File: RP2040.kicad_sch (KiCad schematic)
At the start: 33 parts, among them J1 USB_B_Micro, J2 Conn_01x03, SW1 SW_Push, SW2 SW_Push, U1 AMS1117-3.3, U5 W25Q128JVS, U6 RP2040, Y1 X322512MSB4SI

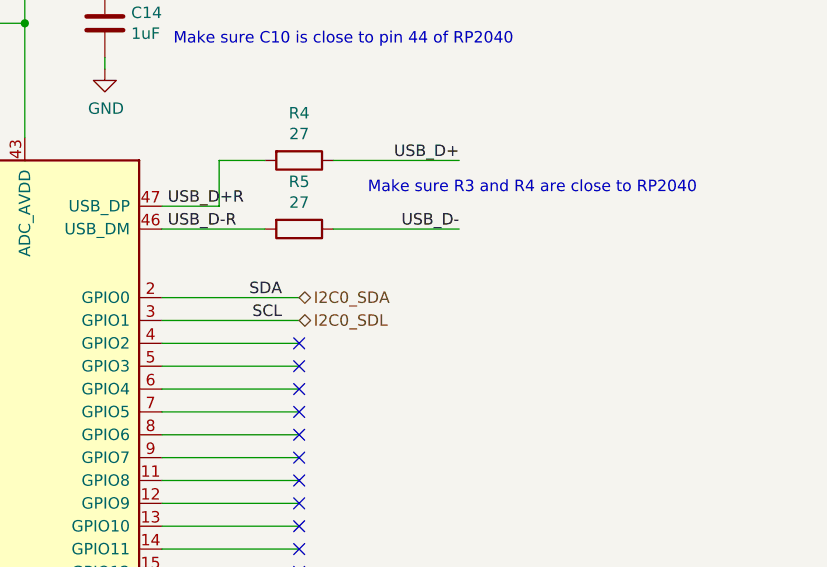
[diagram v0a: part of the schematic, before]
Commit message: Add TCA8418
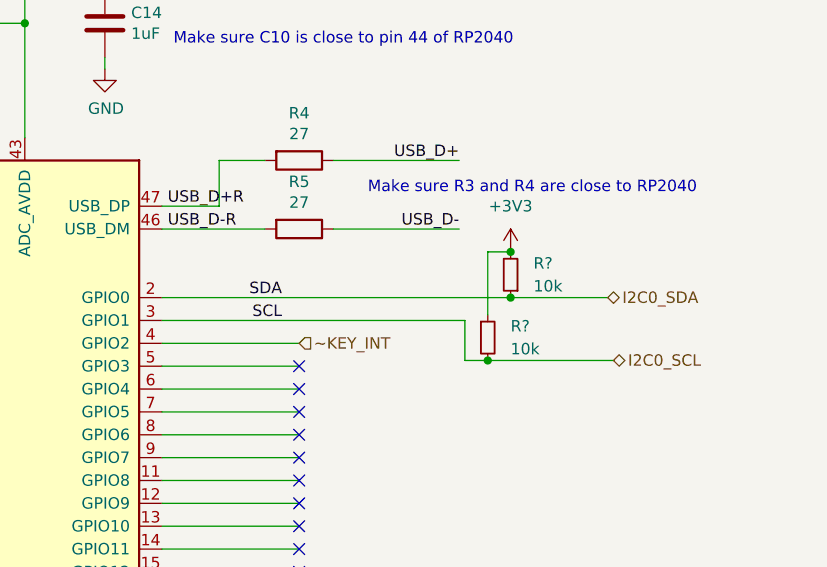
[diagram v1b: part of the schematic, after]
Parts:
- added R? (x2): 10k, symbol Device:R_Small
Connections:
- net +3V3: now also R?.1, R?.2
- net I2C0_SDA: now also R?.1
- net ~KEY_INT: now reaches U6.4 (GPIO2)
- net I2C0_SDL renamed I2C0_SCL
- net I2C0_SCL: now also R?.2
- no-connect marks 29 -> 28
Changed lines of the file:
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@@
   (junction (at 197.485 21.59) (diameter 0) (color 0 0 0 0)
   )
+  (junction (at 248.92 79.375) (diameter 0) (color 0 0 0 0)
+  )
   (junction (at 197.485 41.91) (diameter 0) (color 0 0 0 0)
   )
   (junction (at 182.245 41.91) (diameter 0) (color 0 0 0 0)
   )
+  (junction (at 251.46 72.39) (diameter 0) (color 0 0 0 0)
+  )
   (junction (at 40.005 152.4) (diameter 0) (color 0 0 0 0)
   )
@@
   )
   (junction (at 74.93 65.405) (diameter 0) (color 0 0 0 0)
+  )
+  (junction (at 251.46 67.31) (diameter 0) (color 0 0 0 0)
   )
   (junction (at 263.525 21.59) (diameter 0) (color 0 0 0 0)
@@
   (no_connect (at 29.845 34.925))
   (no_connect (at 227.965 118.11))
-  (no_connect (at 227.965 77.47))
   (no_connect (at 227.965 148.59))
   (no_connect (at 227.965 115.57))
@@
     (stroke (width 0) (type default) (color 0 0 0 0))
   )
-  (wire (pts (xy 212.725 72.39) (xy 227.965 72.39))
+  (wire (pts (xy 212.725 72.39) (xy 251.46 72.39))
     (stroke (width 0) (type default) (color 0 0 0 0))
   )
@@
     (stroke (width 0) (type default) (color 0 0 0 0))
   )
+  (wire (pts (xy 248.92 67.31) (xy 251.46 67.31))
+    (stroke (width 0) (type default) (color 0 0 0 0))
+  )
   (polyline (pts (xy 14.605 107.95) (xy 14.605 130.81))
     (stroke (width 0) (type default) (color 0 0 0 0))
@@
     (stroke (width 0) (type default) (color 0 0 0 0))
   )
+  (wire (pts (xy 251.46 72.39) (xy 262.255 72.39))
+    (stroke (width 0) (type default) (color 0 0 0 0))
+  )
   (wire (pts (xy 219.075 57.15) (xy 224.155 57.15))
     (stroke (width 0) (type default) (color 0 0 0 0))
@@
     (stroke (width 0) (type default) (color 0 0 0 0))
   )
+  (wire (pts (xy 248.92 74.295) (xy 248.92 67.31))
+    (stroke (width 0) (type default) (color 0 0 0 0))
+  )
   (polyline (pts (xy 14.605 103.505) (xy 106.045 103.505))
     (stroke (width 0) (type default) (color 0 0 0 0))
@@
     (stroke (width 0) (type default) (color 0 0 0 0))
   )
+  (wire (pts (xy 246.38 79.375) (xy 248.92 79.375))
+    (stroke (width 0) (type default) (color 0 0 0 0))
+  )
   (wire (pts (xy 19.685 40.005) (xy 19.685 41.275))
     (stroke (width 0) (type default) (color 0 0 0 0))
@@
     (stroke (width 0) (type default) (color 0 0 0 0))
   )
+  (wire (pts (xy 248.92 79.375) (xy 262.89 79.375))
+    (stroke (width 0) (type default) (color 0 0 0 0))
+  )
   (wire (pts (xy 212.725 90.17) (xy 227.965 90.17))
     (stroke (width 0) (type default) (color 0 0 0 0))
@@
     (stroke (width 0) (type default) (color 0 0 0 0))
   )
-  (wire (pts (xy 212.725 74.93) (xy 227.965 74.93))
+  (wire (pts (xy 212.725 74.93) (xy 246.38 74.93))
     (stroke (width 0) (type default) (color 0 0 0 0))
   )
@@
   )
   (wire (pts (xy 212.725 115.57) (xy 227.965 115.57))
+    (stroke (width 0) (type default) (color 0 0 0 0))
+  )
+  (wire (pts (xy 246.38 74.93) (xy 246.38 79.375))
     (stroke (width 0) (type default) (color 0 0 0 0))
   )
@@
     (effects (font (size 1.27 1.27)) (justify left bottom))
   )
-  (hierarchical_label "I2C0_SDA" (shape bidirectional) (at 227.965 72.39 0)
+  (hierarchical_label "~KEY_INT" (shape input) (at 227.965 77.47 0)
     (effects (font (size 1.27 1.27)) (justify left))
   )
-  (hierarchical_label "I2C0_SDL" (shape bidirectional) (at 227.965 74.93 0)
+  (hierarchical_label "I2C0_SDA" (shape bidirectional) (at 262.255 72.39 0)
+    (effects (font (size 1.27 1.27)) (justify left))
+  )
+  (hierarchical_label "I2C0_SCL" (shape bidirectional) (at 262.89 79.375 0)
     (effects (font (size 1.27 1.27)) (justify left))
   )
@@
     )
     (property "Datasheet" "~" (id 3) (at 99.695 138.43 0)
+      (effects (font (size 1.27 1.27)) hide)
+    )
+    (pin "1")
+  )
+  (symbol (lib_id "Device:R_Small") (at 251.46 69.85 180) (unit 1)
+    (in_bom yes) (on_board yes) (fields_autoplaced)
+    (property "Reference" "R?" (id 0) (at 254 68.5799 0)
+      (effects (font (size 1.27 1.27)) (justify right))
+    )
+    (property "Value" "10k" (id 1) (at 254 71.1199 0)
+      (effects (font (size 1.27 1.27)) (justify right))
+    )
+    (property "Footprint" "" (id 2) (at 251.46 69.85 0)
+      (effects (font (size 1.27 1.27)) hide)
+    )
+    (property "Datasheet" "~" (id 3) (at 251.46 69.85 0)
+      (effects (font (size 1.27 1.27)) hide)
+    )
+    (pin "1")
+    (pin "2")
+  )
+  (symbol (lib_id "power:+3V3") (at 251.46 67.31 0) (unit 1)
+    (in_bom yes) (on_board yes) (fields_autoplaced)
+    (property "Reference" "#PWR?" (id 0) (at 251.46 71.12 0)
+      (effects (font (size 1.27 1.27)) hide)
+    )
+    (property "Value" "+3V3" (id 1) (at 251.46 62.23 0))
+    (property "Footprint" "" (id 2) (at 251.46 67.31 0)
+      (effects (font (size 1.27 1.27)) hide)
+    )
+    (property "Datasheet" "" (id 3) (at 251.46 67.31 0)
       (effects (font (size 1.27 1.27)) hide)
     )
@@
       (effects (font (size 1.27 1.27)) hide)
     )
+    (pin "1")
+    (pin "2")
+  )
+  (symbol (lib_id "Device:R_Small") (at 248.92 76.835 0) (unit 1)
+    (in_bom yes) (on_board yes) (fields_autoplaced)
+    (property "Reference" "R?" (id 0) (at 251.46 75.5649 0)
+      (effects (font (size 1.27 1.27)) (justify left))
+    )
+    (property "Value" "10k" (id 1) (at 251.46 78.1049 0)
+      (effects (font (size 1.27 1.27)) (justify left))
+    )
+    (property "Footprint" "" (id 2) (at 248.92 76.835 0)
+      (effects (font (size 1.27 1.27)) hide)
+    )
+    (property "Datasheet" "~" (id 3) (at 248.92 76.835 0)
+      (effects (font (size 1.27 1.27)) hide)
+    )

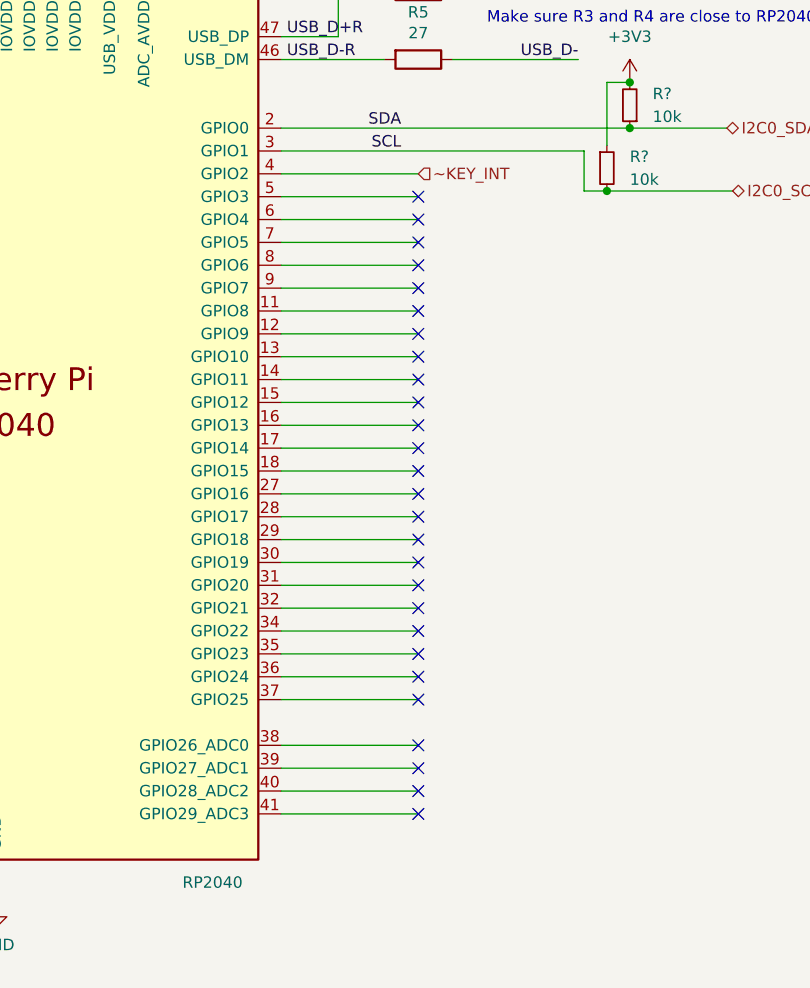
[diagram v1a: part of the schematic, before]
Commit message: Expose the GPIO pins
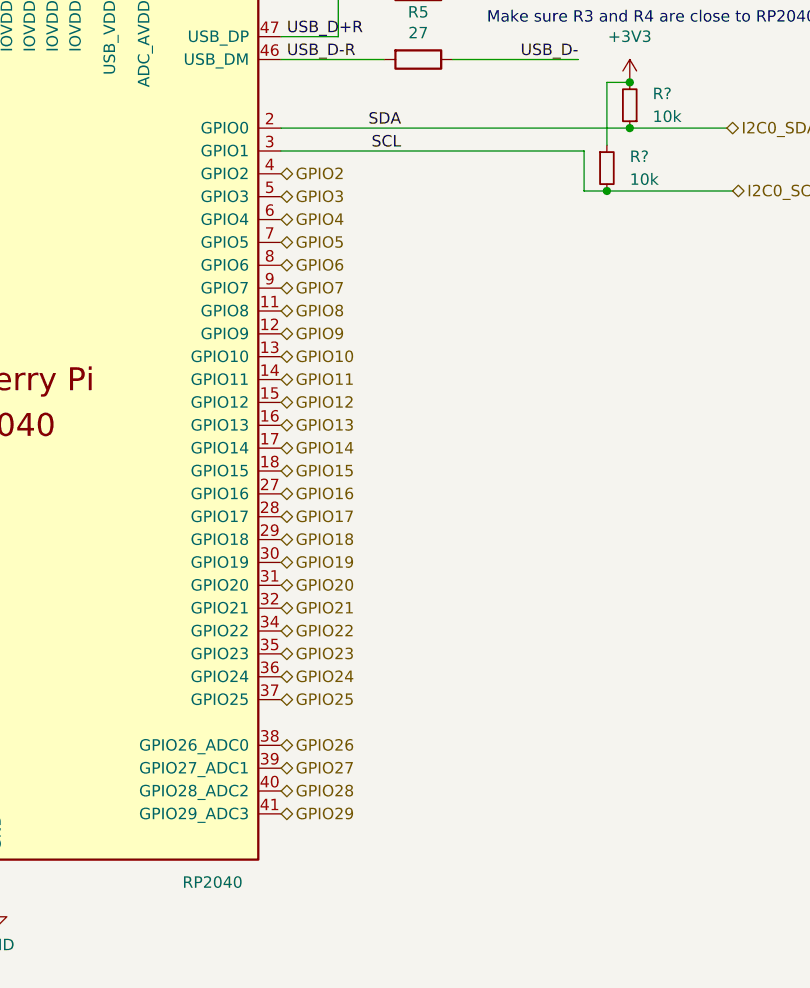
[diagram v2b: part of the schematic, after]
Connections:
- net GPIO8: now reaches U6.11 (GPIO8)
- net GPIO9: now reaches U6.12 (GPIO9)
- net GPIO10: now reaches U6.13 (GPIO10)
- net GPIO11: now reaches U6.14 (GPIO11)
- net GPIO12: now reaches U6.15 (GPIO12)
- net GPIO13: now reaches U6.16 (GPIO13)
- net GPIO14: now reaches U6.17 (GPIO14)
- net GPIO15: now reaches U6.18 (GPIO15)
- net GPIO16: now reaches U6.27 (GPIO16)
- net GPIO17: now reaches U6.28 (GPIO17)
- net GPIO18: now reaches U6.29 (GPIO18)
- net GPIO19: now reaches U6.30 (GPIO19)
- net GPIO20: now reaches U6.31 (GPIO20)
- net GPIO21: now reaches U6.32 (GPIO21)
- net GPIO22: now reaches U6.34 (GPIO22)
- net GPIO23: now reaches U6.35 (GPIO23)
- net GPIO24: now reaches U6.36 (GPIO24)
- net GPIO25: now reaches U6.37 (GPIO25)
- net GPIO26: now reaches U6.38 (GPIO26_ADC0)
- net GPIO27: now reaches U6.39 (GPIO27_ADC1)
- net GPIO28: now reaches U6.40 (GPIO28_ADC2)
- net GPIO29: now reaches U6.41 (GPIO29_ADC3)
- net GPIO3: now reaches U6.5 (GPIO3)
- net GPIO4: now reaches U6.6 (GPIO4)
- net GPIO5: now reaches U6.7 (GPIO5)
- net GPIO6: now reaches U6.8 (GPIO6)
- net GPIO7: now reaches U6.9 (GPIO7)
- net ~KEY_INT renamed GPIO2
- no-connect marks 28 -> 1

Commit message: Initial schematic complete
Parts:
- removed R? (x2): 10k, symbol Device:R_Small
- removed TP1, TP2, TP3: TestPoint, symbol Connector:TestPoint
- C10, C11, C12, C13, C14, C15, C16, C17, C18, C19, C20, C5, C6, C8, R1, R2: footprint Collins-FMS-3000:Perfect_0402 -> Custom_Footprints:Perfect_0402
- J1: footprint Collins-FMS-3000:USB_B_Mini_Amphenol_UE25BE5510H -> Custom_Footprints:USB_B_Mini_Amphenol_UE25BE5510H
- J2: footprint (none) -> Connector_JST:JST_XH_B3B-XH-A_1x03_P2.50mm_Vertical
- R6: footprint (none) -> Custom_Footprints:Perfect_0402
- SW1, SW2: footprint (none) -> Button_Switch_SMD:SW_Push_1P1T_NO_6x6mm_H9.5mm
- U6: footprint RP2040_minimal:RP2040-QFN-56 -> Custom_Footprints:QFN-56-1EP_7x7mm_P0.4mm_EP3.2x3.2mm; symbol MCU_RaspberryPi_RP2040:RP2040 -> Custom_Symbols:RP2040
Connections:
- net I2C0_SCL renamed GPIO1
- net I2C0_SDA renamed GPIO0
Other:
- note added: "Use GPIO0 for I2C0_SDA Use GPIO1 for I2C0_SDL"
- note removed: "Test points"

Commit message: More updates
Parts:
- J2: footprint Connector_JST:JST_XH_B3B-XH-A_1x03_P2.50mm_Vertical -> Connector_PinHeader_2.54mm:PinHeader_1x03_P2.54mm_Vertical
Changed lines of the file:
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@@
       (effects (font (size 1.27 1.27)) (justify left))
     )
-    (property "Footprint" "Connector_JST:JST_XH_B3B-XH-A_1x03_P2.50mm_Vertical" (id 2) (at 60.96 113.665 0)
+    (property "Footprint" "Connector_PinHeader_2.54mm:PinHeader_1x03_P2.54mm_Vertical" (id 2) (at 60.96 113.665 0)
       (effects (font (size 1.27 1.27)) hide)
     )

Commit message: Some board layout work
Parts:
- SW1, SW2: footprint Button_Switch_SMD:SW_Push_1P1T_NO_6x6mm_H9.5mm -> Button_Switch_SMD:SW_SPST_TL3342
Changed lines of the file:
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@@
     (property "Reference" "SW2" (id 0) (at 34.925 115.57 0))
     (property "Value" "SW_Push" (id 1) (at 34.925 118.11 0))
-    (property "Footprint" "Button_Switch_SMD:SW_Push_1P1T_NO_6x6mm_H9.5mm" (id 2) (at 34.925 118.745 0)
+    (property "Footprint" "Button_Switch_SMD:SW_SPST_TL3342" (id 2) (at 34.925 118.745 0)
       (effects (font (size 1.27 1.27)) hide)
     )
@@
     (property "Reference" "SW1" (id 0) (at 22.86 77.47 0))
     (property "Value" "SW_Push" (id 1) (at 22.86 80.01 0))
-    (property "Footprint" "Button_Switch_SMD:SW_Push_1P1T_NO_6x6mm_H9.5mm" (id 2) (at 22.86 80.645 0)
-      (effects (font (size 1.27 1.27)) hide)
-    )
+    (property "Footprint" "Button_Switch_SMD:SW_SPST_TL3342" (id 2) (at 22.86 80.645 0)
+      (effects (font (size 1.27 1.27)) hide)
+    )
